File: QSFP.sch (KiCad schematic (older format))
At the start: 21 parts, among them J17 SAMTEC_QSFP8-038-01-L-D-RA1

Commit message: FMC HPC & LPC done, FPGA power delivery done, RGMII lines done,  MGT lines progress
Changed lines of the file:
@@
 $Descr A4 11693 8268
 encoding utf-8
-Sheet 28 25
+Sheet 17 25
 Title ""
 Date ""
@@
 Text HLabel 9850 4500 2    50   BiDi ~ 0
 QSFP_SDA
-Text Label 6250 1650 0    50   ~ 10
+Text Label 6200 2050 0    50   ~ 10
 MGT_TX_1_P
-Text Label 6250 1750 0    50   ~ 10
+Text Label 6200 1950 0    50   ~ 10
 MGT_TX_1_N
-Text Label 8550 2850 0    50   ~ 10
+Text Label 8500 3150 0    50   ~ 10
 MGT_TX_2_P
-Text Label 8550 2950 0    50   ~ 10
+Text Label 8500 3250 0    50   ~ 10
 MGT_TX_2_N
-Text Label 6250 1950 0    50   ~ 10
+Text Label 8950 2850 2    50   ~ 10
 MGT_TX_3_P
-Text Label 6250 2050 0    50   ~ 10
+Text Label 8950 2950 2    50   ~ 10
 MGT_TX_3_N
-Text Label 6250 3150 0    50   ~ 10
+Text Label 8950 1750 2    50   ~ 10
 MGT_RX_0_P
-Text Label 6250 3250 0    50   ~ 10
+Text Label 8950 1650 2    50   ~ 10
 MGT_RX_0_N
-Text Label 8550 1650 0    50   ~ 10
+Text Label 8500 2050 0    50   ~ 10
 MGT_RX_1_P
-Text Label 8550 1750 0    50   ~ 10
+Text Label 8500 1950 0    50   ~ 10
 MGT_RX_1_N
-Text Label 6250 2850 0    50   ~ 10
+Text Label 6200 3150 0    50   ~ 10
 MGT_RX_2_P
-Text Label 6250 2950 0    50   ~ 10
+Text Label 6200 3250 0    50   ~ 10
 MGT_RX_2_N
-Text Label 8550 1950 0    50   ~ 10
+Text Label 6650 2850 2    50   ~ 10
 MGT_RX_3_P
-Text Label 8550 2050 0    50   ~ 10
+Text Label 6650 2950 2    50   ~ 10
 MGT_RX_3_N
-Text Label 8550 3250 0    50   ~ 10
+Text Label 6650 1650 2    50   ~ 10
 MGT_TX_0_N
-Text Label 8550 3150 0    50   ~ 10
+Text Label 6650 1750 2    50   ~ 10
 MGT_TX_0_P
+Text HLabel 6050 1750 0    50   Input ~ 10
+MGT_TX_0_P
+Text HLabel 6050 1650 0    50   Input ~ 10
+MGT_TX_0_N
+Text HLabel 6050 2050 0    50   Input ~ 10
+MGT_TX_1_P
+Text HLabel 6050 1950 0    50   Input ~ 10
+MGT_TX_1_N
 Text HLabel 9150 3150 2    50   Input ~ 10
-MGT_TX_0_P
+MGT_TX_2_P
 Text HLabel 9150 3250 2    50   Input ~ 10
-MGT_TX_0_N
-Text HLabel 6050 1650 0    50   Input ~ 10
-MGT_TX_1_P
-Text HLabel 6050 1750 0    50   Input ~ 10
-MGT_TX_1_N
+MGT_TX_2_N
 Text HLabel 9150 2850 2    50   Input ~ 10
-MGT_TX_2_P
+MGT_TX_3_P
 Text HLabel 9150 2950 2    50   Input ~ 10
-MGT_TX_2_N
-Text HLabel 6050 1950 0    50   Input ~ 10
-MGT_TX_3_P
-Text HLabel 6050 2050 0    50   Input ~ 10
 MGT_TX_3_N
+Text HLabel 9150 1750 2    50   Output ~ 10
+MGT_RX_0_P
+Text HLabel 9150 1650 2    50   Output ~ 10
+MGT_RX_0_N
+Text HLabel 9150 2050 2    50   Output ~ 10
+MGT_RX_1_P
+Text HLabel 9150 1950 2    50   Output ~ 10
+MGT_RX_1_N
 Text HLabel 6050 3150 0    50   Output ~ 10
-MGT_RX_0_P
+MGT_RX_2_P
 Text HLabel 6050 3250 0    50   Output ~ 10
-MGT_RX_0_N
-Text HLabel 9150 1650 2    50   Output ~ 10
-MGT_RX_1_P
-Text HLabel 9150 1750 2    50   Output ~ 10
-MGT_RX_1_N
+MGT_RX_2_N
 Text HLabel 6050 2850 0    50   Output ~ 10
-MGT_RX_2_P
+MGT_RX_3_P
 Text HLabel 6050 2950 0    50   Output ~ 10
-MGT_RX_2_N
-Text HLabel 9150 1950 2    50   Output ~ 10
-MGT_RX_3_P
-Text HLabel 9150 2050 2    50   Output ~ 10
 MGT_RX_3_N
 Wire Wire Line
-	6050 1650 6900 1650
-Wire Wire Line
-	6050 1750 6900 1750
+	6050 2050 6900 2050
 Wire Wire Line
 	6050 1950 6900 1950
 Wire Wire Line
-	6050 2050 6900 2050
-Wire Wire Line
-	6050 2850 6900 2850
-Wire Wire Line
-	6050 2950 6900 2950
+	9150 2850 8300 2850
+Wire Wire Line
+	9150 2950 8300 2950
 Wire Wire Line
 	6050 3150 6900 3150
@@
 	6050 3250 6900 3250
 Wire Wire Line
-	8300 2850 9150 2850
-Wire Wire Line
-	8300 2950 9150 2950
+	9150 1750 8300 1750
+Wire Wire Line
+	9150 1650 8300 1650
 Wire Wire Line
 	8300 3150 9150 3150
@@
 	8300 3250 9150 3250
 Wire Wire Line
-	8300 1650 9150 1650
-Wire Wire Line
-	8300 1750 9150 1750
+	6900 1750 6050 1750
+Wire Wire Line
+	6900 1650 6050 1650
+Wire Wire Line
+	8300 2050 9150 2050
 Wire Wire Line
 	8300 1950 9150 1950
 Wire Wire Line
-	8300 2050 9150 2050
+	6900 2850 6050 2850
+Wire Wire Line
+	6900 2950 6050 2950
 Connection ~ 9650 2250
 Wire Wire Line

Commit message: new board outline, rearranging banks connections, SODIMM memory
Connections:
- net labels added: QSFP_RX_0_N, QSFP_RX_0_P, QSFP_RX_1_N, QSFP_RX_1_P, QSFP_RX_2_N, QSFP_RX_2_P, QSFP_RX_3_N, QSFP_RX_3_P, QSFP_TX_0_N, QSFP_TX_0_P, QSFP_TX_1_N, QSFP_TX_1_P, QSFP_TX_2_N, QSFP_TX_2_P, QSFP_TX_3_N, QSFP_TX_3_P
- net labels removed: MGT_RX_0_N, MGT_RX_0_P, MGT_RX_1_N, MGT_RX_1_P, MGT_RX_2_N, MGT_RX_2_P, MGT_RX_3_N, MGT_RX_3_P, MGT_TX_0_N, MGT_TX_0_P, MGT_TX_1_N, MGT_TX_1_P, MGT_TX_2_N, MGT_TX_2_P, MGT_TX_3_N, MGT_TX_3_P

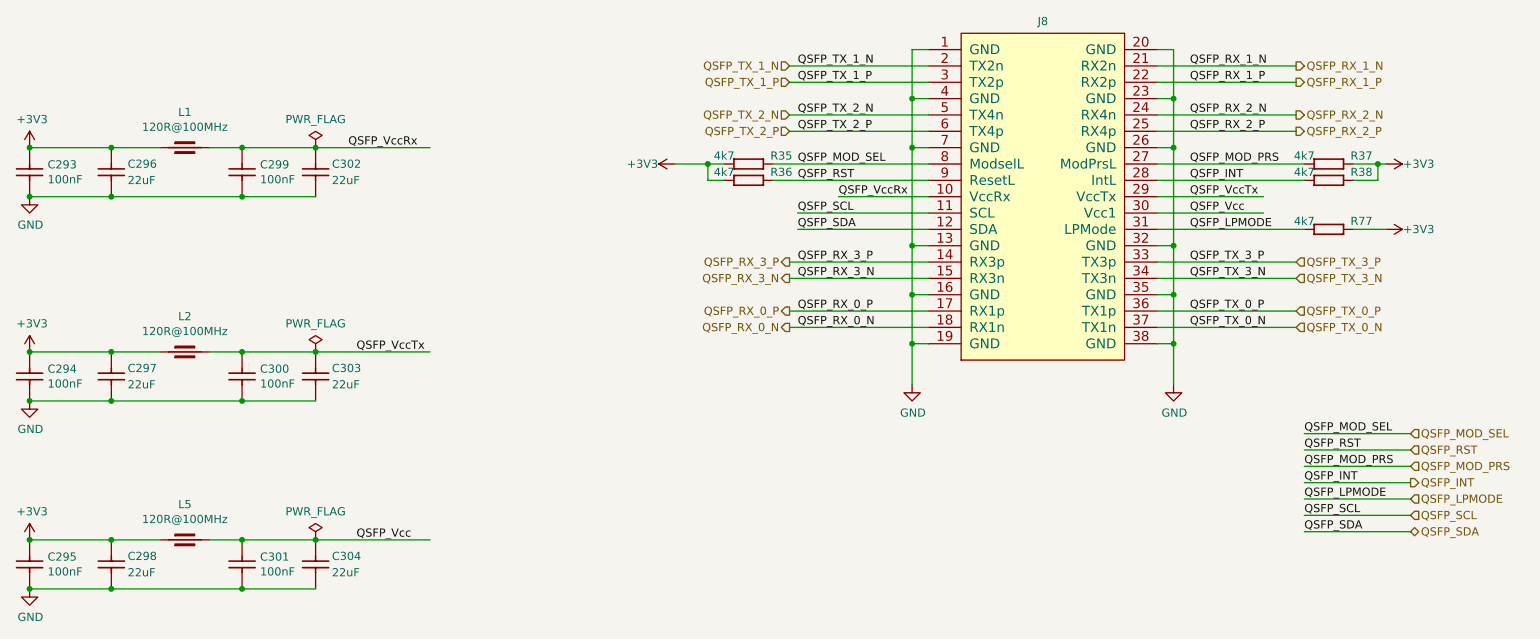
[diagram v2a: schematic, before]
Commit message: FMC2 routing done
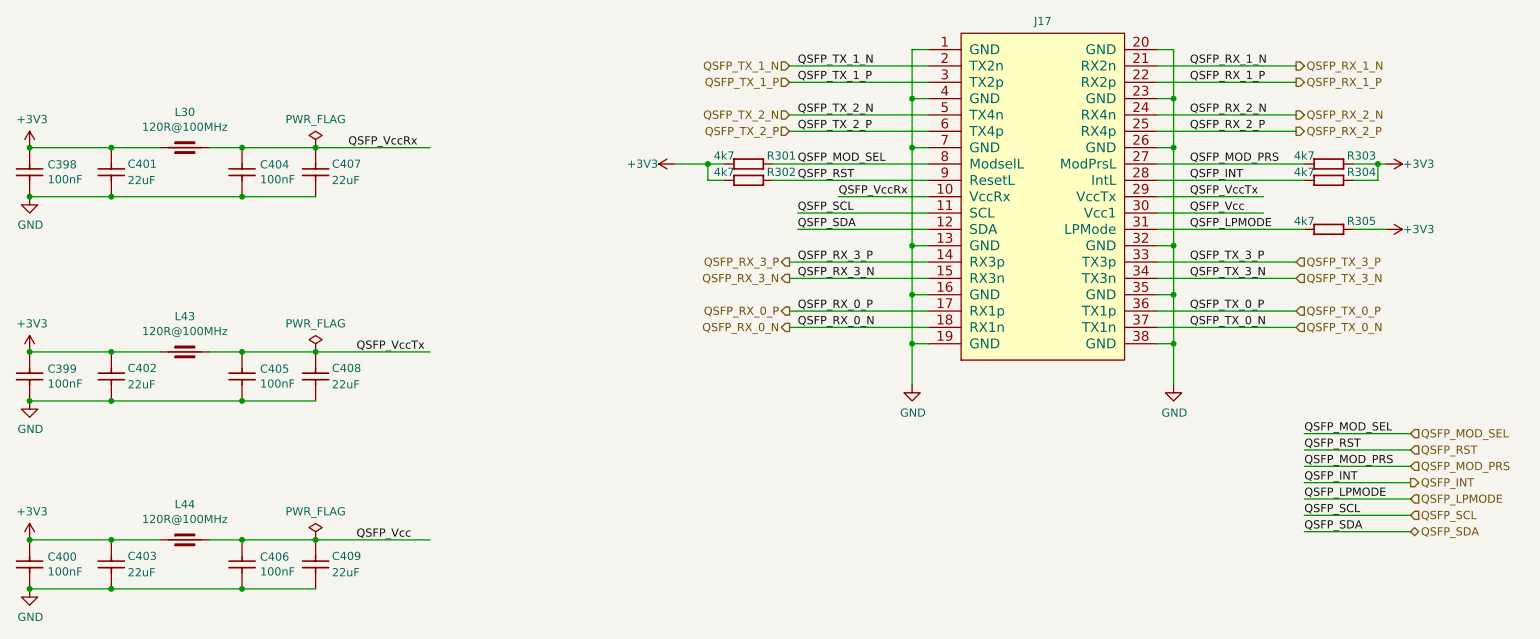
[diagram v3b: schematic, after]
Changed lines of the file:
@@
 $Descr A4 11693 8268
 encoding utf-8
-Sheet 16 25
+Sheet 15 25
 Title ""
 Date ""
@@
 AR Path="/600349C1/5E836B5E" Ref="J?"  Part="1"
 AR Path="/60326218/5E836B5E" Ref="J8"  Part="1"
-F 0 "J8" H 7600 1523 50  0000 C CNN
+F 0 "J17" H 7600 1523 50  0000 C CNN
 F 1 "SAMTEC_QSFP8-038-01-L-D-RA1" H 7100 -625 50  0001 L CNN
 F 2 "SAMTEC SMD:SAMTEC_QSFP8-038-01-L-D-RA1" H 7100 -700 50  0001 L CNN
@@
 AR Path="/600349C1/5E847880" Ref="C?"  Part="1"
 AR Path="/60326218/5E847880" Ref="C293"  Part="1"
-F 0 "C293" V 1504 2260 50  0000 L CNN
+F 0 "C398" V 1504 2260 50  0000 L CNN
 F 1 "CC0201_100NF_6.3V_10%_X5R" H 1400 1890 60  0001 L CNN
 F 2 "CAPC0603X33N" H 1400 1080 60  0001 L CNN
@@
 AR Path="/600349C1/5E8478AB" Ref="C?"  Part="1"
 AR Path="/60326218/5E8478AB" Ref="C299"  Part="1"
-F 0 "C299" V 2804 2260 50  0000 L CNN
+F 0 "C404" V 2804 2260 50  0000 L CNN
 F 1 "CC0201_100NF_6.3V_10%_X5R" H 2700 1890 60  0001 L CNN
 F 2 "CAPC0603X33N" H 2700 1080 60  0001 L CNN
@@
 AR Path="/600349C1/5E8478DA" Ref="L?"  Part="1"
 AR Path="/60326218/5E8478DA" Ref="L1"  Part="1"
-F 0 "L1" H 2350 2367 50  0000 C CNN
+F 0 "L30" H 2350 2367 50  0000 C CNN
 F 1 "IND0603_MURATA_BLM18SG121TN1D" H 2200 1960 60  0001 L CNN
 F 2 "INDC1608X65N" H 2200 1150 60  0001 L CNN
@@
 AR Path="/600349C1/5E858016" Ref="R?"  Part="1"
 AR Path="/60326218/5E858016" Ref="R37"  Part="1"
-F 0 "R37" H 9550 2300 50  0000 C CNN
+F 0 "R303" H 9550 2300 50  0000 C CNN
 F 1 "R0402_4K7_1%_0.0625W_100PPM" H 9200 2055 50  0001 L CNN
 F 2 "Resistors SMD:RESC1005X40N" H 9200 1980 50  0001 L CNN
@@
 AR Path="/600349C1/5E85CEDE" Ref="R?"  Part="1"
 AR Path="/60326218/5E85CEDE" Ref="R38"  Part="1"
-F 0 "R38" H 9550 2400 50  0000 C CNN
+F 0 "R304" H 9550 2400 50  0000 C CNN
 F 1 "R0402_4K7_1%_0.0625W_100PPM" H 9200 2155 50  0001 L CNN
 F 2 "Resistors SMD:RESC1005X40N" H 9200 2080 50  0001 L CNN
@@
 AR Path="/600349C1/5E85EA84" Ref="R?"  Part="1"
 AR Path="/60326218/5E85EA84" Ref="R77"  Part="1"
-F 0 "R77" H 9550 2700 50  0000 C CNN
+F 0 "R305" H 9550 2700 50  0000 C CNN
 F 1 "R0402_4K7_1%_0.0625W_100PPM" H 9200 2455 50  0001 L CNN
 F 2 "Resistors SMD:RESC1005X40N" H 9200 2380 50  0001 L CNN
@@
 AR Path="/600349C1/5E8613D4" Ref="R?"  Part="1"
 AR Path="/60326218/5E8613D4" Ref="R35"  Part="1"
-F 0 "R35" H 6000 2300 50  0000 C CNN
+F 0 "R301" H 6000 2300 50  0000 C CNN
 F 1 "R0402_4K7_1%_0.0625W_100PPM" H 5650 2055 50  0001 L CNN
 F 2 "Resistors SMD:RESC1005X40N" H 5650 1980 50  0001 L CNN
@@
 AR Path="/600349C1/5E862709" Ref="R?"  Part="1"
 AR Path="/60326218/5E862709" Ref="R36"  Part="1"
-F 0 "R36" H 6000 2400 50  0000 C CNN
+F 0 "R302" H 6000 2400 50  0000 C CNN
 F 1 "R0402_4K7_1%_0.0625W_100PPM" H 5650 2155 50  0001 L CNN
 F 2 "Resistors SMD:RESC1005X40N" H 5650 2080 50  0001 L CNN
@@
 AR Path="/600349C1/5E97F560" Ref="C?"  Part="1"
 AR Path="/60326218/5E97F560" Ref="C302"  Part="1"
-F 0 "C302" V 3250 2250 50  0000 L CNN
+F 0 "C407" V 3250 2250 50  0000 L CNN
 F 1 "CC0603_22UF_6.3V_20%_X5R" H 3150 1890 60  0001 L CNN
 F 2 "CAPC1709X100N" H 3150 1080 60  0001 L CNN
@@
 AR Path="/600349C1/5E9817AE" Ref="C?"  Part="1"
 AR Path="/60326218/5E9817AE" Ref="C296"  Part="1"
-F 0 "C296" V 2000 2250 50  0000 L CNN
+F 0 "C401" V 2000 2250 50  0000 L CNN
 F 1 "CC0603_22UF_6.3V_20%_X5R" H 1900 1890 60  0001 L CNN
 F 2 "CAPC1709X100N" H 1900 1080 60  0001 L CNN
@@
 AR Path="/600349C1/5E9CDCAF" Ref="C?"  Part="1"
 AR Path="/60326218/5E9CDCAF" Ref="C294"  Part="1"
-F 0 "C294" V 1504 3510 50  0000 L CNN
+F 0 "C399" V 1504 3510 50  0000 L CNN
 F 1 "CC0201_100NF_6.3V_10%_X5R" H 1400 3140 60  0001 L CNN
 F 2 "CAPC0603X33N" H 1400 2330 60  0001 L CNN
@@
 AR Path="/600349C1/5E9CDCDA" Ref="C?"  Part="1"
 AR Path="/60326218/5E9CDCDA" Ref="C300"  Part="1"
-F 0 "C300" V 2804 3510 50  0000 L CNN
+F 0 "C405" V 2804 3510 50  0000 L CNN
 F 1 "CC0201_100NF_6.3V_10%_X5R" H 2700 3140 60  0001 L CNN
 F 2 "CAPC0603X33N" H 2700 2330 60  0001 L CNN
@@
 AR Path="/600349C1/5E9CDD01" Ref="L?"  Part="1"
 AR Path="/60326218/5E9CDD01" Ref="L2"  Part="1"
-F 0 "L2" H 2350 3617 50  0000 C CNN
+F 0 "L43" H 2350 3617 50  0000 C CNN
 F 1 "IND0603_MURATA_BLM18SG121TN1D" H 2200 3210 60  0001 L CNN
 F 2 "INDC1608X65N" H 2200 2400 60  0001 L CNN
@@
 AR Path="/600349C1/5E9CDD2C" Ref="C?"  Part="1"
 AR Path="/60326218/5E9CDD2C" Ref="C303"  Part="1"
-F 0 "C303" V 3250 3500 50  0000 L CNN
+F 0 "C408" V 3250 3500 50  0000 L CNN
 F 1 "CC0603_22UF_6.3V_20%_X5R" H 3150 3140 60  0001 L CNN
 F 2 "CAPC1709X100N" H 3150 2330 60  0001 L CNN
@@
 AR Path="/600349C1/5E9CDD57" Ref="C?"  Part="1"
 AR Path="/60326218/5E9CDD57" Ref="C297"  Part="1"
-F 0 "C297" V 2000 3500 50  0000 L CNN
+F 0 "C402" V 2000 3500 50  0000 L CNN
 F 1 "CC0603_22UF_6.3V_20%_X5R" H 1900 3140 60  0001 L CNN
 F 2 "CAPC1709X100N" H 1900 2330 60  0001 L CNN
@@
 AR Path="/600349C1/5E9D2126" Ref="C?"  Part="1"
 AR Path="/60326218/5E9D2126" Ref="C295"  Part="1"
-F 0 "C295" V 1504 4660 50  0000 L CNN
+F 0 "C400" V 1504 4660 50  0000 L CNN
 F 1 "CC0201_100NF_6.3V_10%_X5R" H 1400 4290 60  0001 L CNN
 F 2 "CAPC0603X33N" H 1400 3480 60  0001 L CNN
@@
 AR Path="/600349C1/5E9D2151" Ref="C?"  Part="1"
 AR Path="/60326218/5E9D2151" Ref="C301"  Part="1"
-F 0 "C301" V 2804 4660 50  0000 L CNN
+F 0 "C406" V 2804 4660 50  0000 L CNN
 F 1 "CC0201_100NF_6.3V_10%_X5R" H 2700 4290 60  0001 L CNN
 F 2 "CAPC0603X33N" H 2700 3480 60  0001 L CNN
@@
 AR Path="/600349C1/5E9D2178" Ref="L?"  Part="1"
 AR Path="/60326218/5E9D2178" Ref="L5"  Part="1"
-F 0 "L5" H 2350 4767 50  0000 C CNN
+F 0 "L44" H 2350 4767 50  0000 C CNN
 F 1 "IND0603_MURATA_BLM18SG121TN1D" H 2200 4360 60  0001 L CNN
 F 2 "INDC1608X65N" H 2200 3550 60  0001 L CNN
@@
 AR Path="/600349C1/5E9D21A3" Ref="C?"  Part="1"
 AR Path="/60326218/5E9D21A3" Ref="C304"  Part="1"
-F 0 "C304" V 3250 4650 50  0000 L CNN
+F 0 "C409" V 3250 4650 50  0000 L CNN
 F 1 "CC0603_22UF_6.3V_20%_X5R" H 3150 4290 60  0001 L CNN
 F 2 "CAPC1709X100N" H 3150 3480 60  0001 L CNN
@@
 AR Path="/600349C1/5E9D21CE" Ref="C?"  Part="1"
 AR Path="/60326218/5E9D21CE" Ref="C298"  Part="1"
-F 0 "C298" V 2000 4650 50  0000 L CNN
+F 0 "C403" V 2000 4650 50  0000 L CNN
 F 1 "CC0603_22UF_6.3V_20%_X5R" H 1900 4290 60  0001 L CNN
 F 2 "CAPC1709X100N" H 1900 3480 60  0001 L CNN

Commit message: routing progress
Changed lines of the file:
@@
 AR Path="/600349C1/5E836B5E" Ref="J?"  Part="1"
 AR Path="/60326218/5E836B5E" Ref="J8"  Part="1"
-F 0 "J17" H 7600 1523 50  0000 C CNN
+F 0 "J8" H 7600 1523 50  0000 C CNN
 F 1 "SAMTEC_QSFP8-038-01-L-D-RA1" H 7100 -625 50  0001 L CNN
 F 2 "SAMTEC SMD:SAMTEC_QSFP8-038-01-L-D-RA1" H 7100 -700 50  0001 L CNN
@@
 AR Path="/600349C1/5E847880" Ref="C?"  Part="1"
 AR Path="/60326218/5E847880" Ref="C293"  Part="1"
-F 0 "C398" V 1504 2260 50  0000 L CNN
+F 0 "C293" V 1504 2260 50  0000 L CNN
 F 1 "CC0201_100NF_6.3V_10%_X5R" H 1400 1890 60  0001 L CNN
 F 2 "CAPC0603X33N" H 1400 1080 60  0001 L CNN
@@
 AR Path="/600349C1/5E8478AB" Ref="C?"  Part="1"
 AR Path="/60326218/5E8478AB" Ref="C299"  Part="1"
-F 0 "C404" V 2804 2260 50  0000 L CNN
+F 0 "C299" V 2804 2260 50  0000 L CNN
 F 1 "CC0201_100NF_6.3V_10%_X5R" H 2700 1890 60  0001 L CNN
 F 2 "CAPC0603X33N" H 2700 1080 60  0001 L CNN
@@
 AR Path="/600349C1/5E8478DA" Ref="L?"  Part="1"
 AR Path="/60326218/5E8478DA" Ref="L1"  Part="1"
-F 0 "L30" H 2350 2367 50  0000 C CNN
+F 0 "L1" H 2350 2367 50  0000 C CNN
 F 1 "IND0603_MURATA_BLM18SG121TN1D" H 2200 1960 60  0001 L CNN
 F 2 "INDC1608X65N" H 2200 1150 60  0001 L CNN
@@
 AR Path="/600349C1/5E858016" Ref="R?"  Part="1"
 AR Path="/60326218/5E858016" Ref="R37"  Part="1"
-F 0 "R303" H 9550 2300 50  0000 C CNN
+F 0 "R37" H 9550 2300 50  0000 C CNN
 F 1 "R0402_4K7_1%_0.0625W_100PPM" H 9200 2055 50  0001 L CNN
 F 2 "Resistors SMD:RESC1005X40N" H 9200 1980 50  0001 L CNN
@@
 AR Path="/600349C1/5E85CEDE" Ref="R?"  Part="1"
 AR Path="/60326218/5E85CEDE" Ref="R38"  Part="1"
-F 0 "R304" H 9550 2400 50  0000 C CNN
+F 0 "R38" H 9550 2400 50  0000 C CNN
 F 1 "R0402_4K7_1%_0.0625W_100PPM" H 9200 2155 50  0001 L CNN
 F 2 "Resistors SMD:RESC1005X40N" H 9200 2080 50  0001 L CNN
@@
 AR Path="/600349C1/5E85EA84" Ref="R?"  Part="1"
 AR Path="/60326218/5E85EA84" Ref="R77"  Part="1"
-F 0 "R305" H 9550 2700 50  0000 C CNN
+F 0 "R77" H 9550 2700 50  0000 C CNN
 F 1 "R0402_4K7_1%_0.0625W_100PPM" H 9200 2455 50  0001 L CNN
 F 2 "Resistors SMD:RESC1005X40N" H 9200 2380 50  0001 L CNN
@@
 AR Path="/600349C1/5E8613D4" Ref="R?"  Part="1"
 AR Path="/60326218/5E8613D4" Ref="R35"  Part="1"
-F 0 "R301" H 6000 2300 50  0000 C CNN
+F 0 "R35" H 6000 2300 50  0000 C CNN
 F 1 "R0402_4K7_1%_0.0625W_100PPM" H 5650 2055 50  0001 L CNN
 F 2 "Resistors SMD:RESC1005X40N" H 5650 1980 50  0001 L CNN
@@
 AR Path="/600349C1/5E862709" Ref="R?"  Part="1"
 AR Path="/60326218/5E862709" Ref="R36"  Part="1"
-F 0 "R302" H 6000 2400 50  0000 C CNN
+F 0 "R36" H 6000 2400 50  0000 C CNN
 F 1 "R0402_4K7_1%_0.0625W_100PPM" H 5650 2155 50  0001 L CNN
 F 2 "Resistors SMD:RESC1005X40N" H 5650 2080 50  0001 L CNN
@@
 AR Path="/600349C1/5E97F560" Ref="C?"  Part="1"
 AR Path="/60326218/5E97F560" Ref="C302"  Part="1"
-F 0 "C407" V 3250 2250 50  0000 L CNN
+F 0 "C302" V 3250 2250 50  0000 L CNN
 F 1 "CC0603_22UF_6.3V_20%_X5R" H 3150 1890 60  0001 L CNN
 F 2 "CAPC1709X100N" H 3150 1080 60  0001 L CNN
@@
 AR Path="/600349C1/5E9817AE" Ref="C?"  Part="1"
 AR Path="/60326218/5E9817AE" Ref="C296"  Part="1"
-F 0 "C401" V 2000 2250 50  0000 L CNN
+F 0 "C296" V 2000 2250 50  0000 L CNN
 F 1 "CC0603_22UF_6.3V_20%_X5R" H 1900 1890 60  0001 L CNN
 F 2 "CAPC1709X100N" H 1900 1080 60  0001 L CNN
@@
 AR Path="/600349C1/5E9CDCAF" Ref="C?"  Part="1"
 AR Path="/60326218/5E9CDCAF" Ref="C294"  Part="1"
-F 0 "C399" V 1504 3510 50  0000 L CNN
+F 0 "C294" V 1504 3510 50  0000 L CNN
 F 1 "CC0201_100NF_6.3V_10%_X5R" H 1400 3140 60  0001 L CNN
 F 2 "CAPC0603X33N" H 1400 2330 60  0001 L CNN
@@
 AR Path="/600349C1/5E9CDCDA" Ref="C?"  Part="1"
 AR Path="/60326218/5E9CDCDA" Ref="C300"  Part="1"
-F 0 "C405" V 2804 3510 50  0000 L CNN
+F 0 "C300" V 2804 3510 50  0000 L CNN
 F 1 "CC0201_100NF_6.3V_10%_X5R" H 2700 3140 60  0001 L CNN
 F 2 "CAPC0603X33N" H 2700 2330 60  0001 L CNN
@@
 AR Path="/600349C1/5E9CDD01" Ref="L?"  Part="1"
 AR Path="/60326218/5E9CDD01" Ref="L2"  Part="1"
-F 0 "L43" H 2350 3617 50  0000 C CNN
+F 0 "L2" H 2350 3617 50  0000 C CNN
 F 1 "IND0603_MURATA_BLM18SG121TN1D" H 2200 3210 60  0001 L CNN
 F 2 "INDC1608X65N" H 2200 2400 60  0001 L CNN
@@
 AR Path="/600349C1/5E9CDD2C" Ref="C?"  Part="1"
 AR Path="/60326218/5E9CDD2C" Ref="C303"  Part="1"
-F 0 "C408" V 3250 3500 50  0000 L CNN
+F 0 "C303" V 3250 3500 50  0000 L CNN
 F 1 "CC0603_22UF_6.3V_20%_X5R" H 3150 3140 60  0001 L CNN
 F 2 "CAPC1709X100N" H 3150 2330 60  0001 L CNN
@@
 AR Path="/600349C1/5E9CDD57" Ref="C?"  Part="1"
 AR Path="/60326218/5E9CDD57" Ref="C297"  Part="1"
-F 0 "C402" V 2000 3500 50  0000 L CNN
+F 0 "C297" V 2000 3500 50  0000 L CNN
 F 1 "CC0603_22UF_6.3V_20%_X5R" H 1900 3140 60  0001 L CNN
 F 2 "CAPC1709X100N" H 1900 2330 60  0001 L CNN
@@
 AR Path="/600349C1/5E9D2126" Ref="C?"  Part="1"
 AR Path="/60326218/5E9D2126" Ref="C295"  Part="1"
-F 0 "C400" V 1504 4660 50  0000 L CNN
+F 0 "C295" V 1504 4660 50  0000 L CNN
 F 1 "CC0201_100NF_6.3V_10%_X5R" H 1400 4290 60  0001 L CNN
 F 2 "CAPC0603X33N" H 1400 3480 60  0001 L CNN
@@
 AR Path="/600349C1/5E9D2151" Ref="C?"  Part="1"
 AR Path="/60326218/5E9D2151" Ref="C301"  Part="1"
-F 0 "C406" V 2804 4660 50  0000 L CNN
+F 0 "C301" V 2804 4660 50  0000 L CNN
 F 1 "CC0201_100NF_6.3V_10%_X5R" H 2700 4290 60  0001 L CNN
 F 2 "CAPC0603X33N" H 2700 3480 60  0001 L CNN
@@
 AR Path="/600349C1/5E9D2178" Ref="L?"  Part="1"
 AR Path="/60326218/5E9D2178" Ref="L5"  Part="1"
-F 0 "L44" H 2350 4767 50  0000 C CNN
+F 0 "L5" H 2350 4767 50  0000 C CNN
 F 1 "IND0603_MURATA_BLM18SG121TN1D" H 2200 4360 60  0001 L CNN
 F 2 "INDC1608X65N" H 2200 3550 60  0001 L CNN
@@
 AR Path="/600349C1/5E9D21A3" Ref="C?"  Part="1"
 AR Path="/60326218/5E9D21A3" Ref="C304"  Part="1"
-F 0 "C409" V 3250 4650 50  0000 L CNN
+F 0 "C304" V 3250 4650 50  0000 L CNN
 F 1 "CC0603_22UF_6.3V_20%_X5R" H 3150 4290 60  0001 L CNN
 F 2 "CAPC1709X100N" H 3150 3480 60  0001 L CNN
@@
 AR Path="/600349C1/5E9D21CE" Ref="C?"  Part="1"
 AR Path="/60326218/5E9D21CE" Ref="C298"  Part="1"
-F 0 "C403" V 2000 4650 50  0000 L CNN
+F 0 "C298" V 2000 4650 50  0000 L CNN
 F 1 "CC0603_22UF_6.3V_20%_X5R" H 1900 4290 60  0001 L CNN
 F 2 "CAPC1709X100N" H 1900 3480 60  0001 L CNN
